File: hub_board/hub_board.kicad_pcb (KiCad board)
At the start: 4 copper layers, 75 x 75 mm, 16 parts, among them J1 Fingers, J2 Fingers, J3 Fingers, J4 Fingers, J5 1473149-4, J6 Test Points, J7 54-00166, U1 AP2112K-3.3TRG1

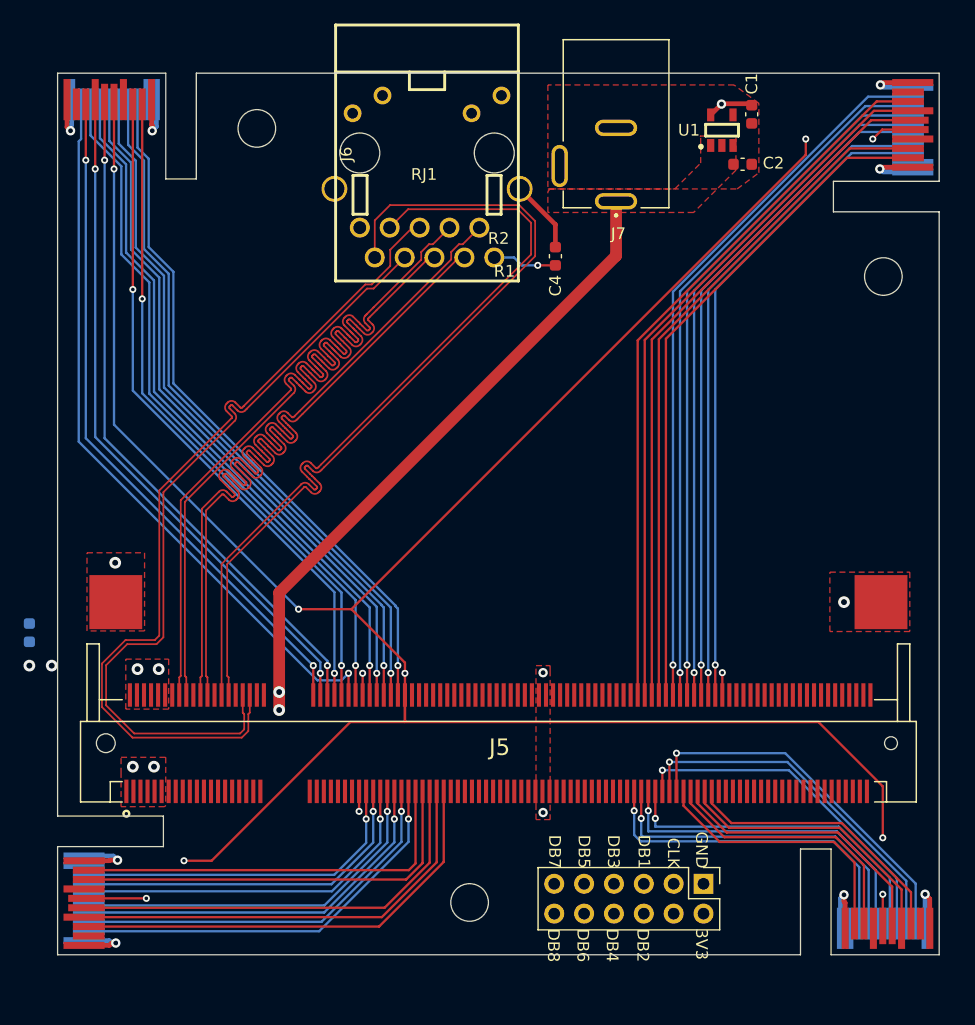
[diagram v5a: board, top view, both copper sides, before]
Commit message: Finish routing hub board
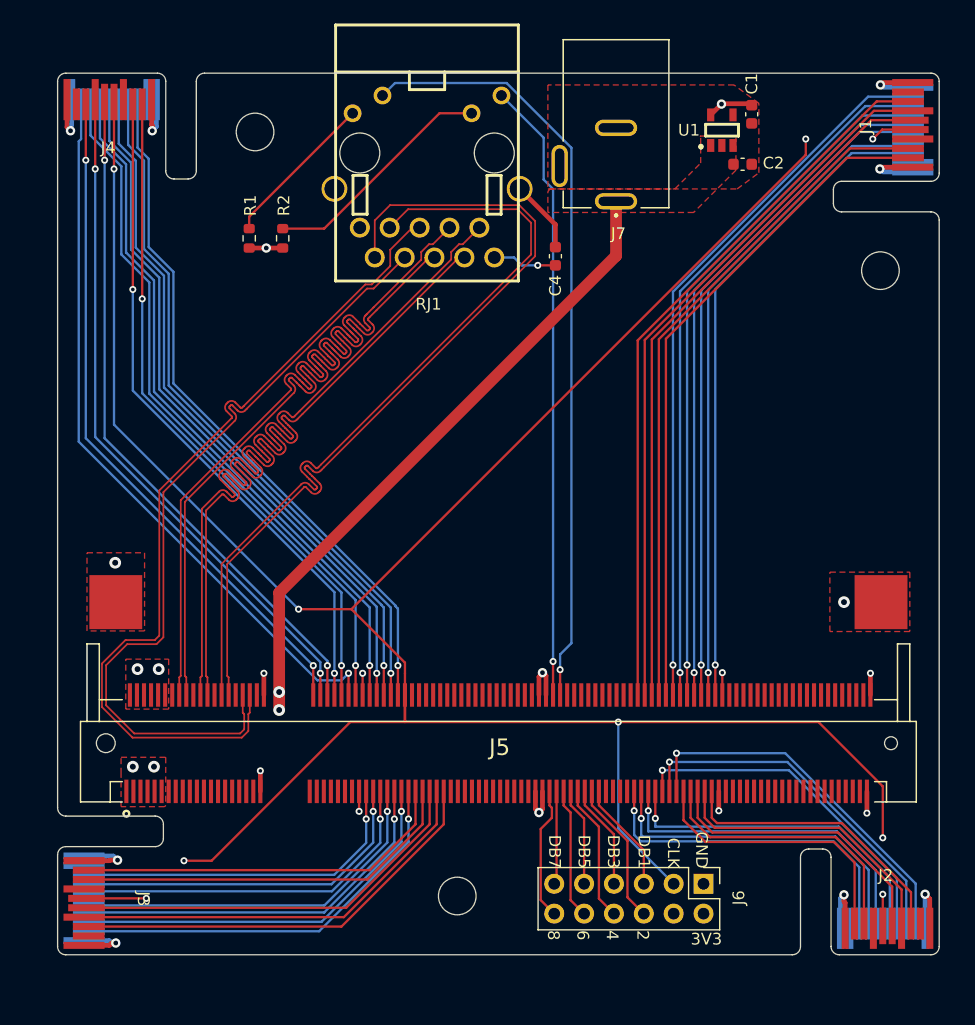
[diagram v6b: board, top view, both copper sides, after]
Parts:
- removed C3: 10u, Capacitor_SMD:C_0603_1608Metric
- added R1: 220, Resistor_SMD:R_0603_1608Metric, F.Cu at (16.3, 14.1)
- added R2: 220, Resistor_SMD:R_0603_1608Metric, F.Cu at (19.1, 14.1)
- moved REF** 1.19 mm to (34.0, 70.0)
- moved REF** 0.56 mm to (70.0, 16.8)
- moved REF** 0.34 mm to (16.8, 5.00)
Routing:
- net /LED1: track 0.00 -> 65.5 mm, vias 0 -> 1
- net /LED2: track 0.00 -> 53.1 mm, vias 0 -> 1
- net Net-(RJ1-LED2+): track 0.00 -> 20.1 mm
- net /CLK: track 220.1 -> 235.8 mm
- net GND: track 35.7 -> 51.0 mm, vias 13 -> 18
- net Net-(RJ1-LED1+): track 0.00 -> 13.5 mm
- net /DBG2: track 0.00 -> 12.2 mm
- net /DBG4: track 0.00 -> 11.7 mm
- net /DBG8: track 0.00 -> 11.4 mm
- net /DBG6: track 0.00 -> 11.1 mm
- net /DBG1: track 0.00 -> 9.44 mm
- net /DBG3: track 0.00 -> 8.89 mm
- net /DBG5: track 0.00 -> 8.33 mm
- net /DBG7: track 0.00 -> 7.94 mm
- net +3V3: track 26.6 -> 29.4 mm, vias 5 -> 6
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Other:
- outline, holes or cut-outs redrawn
- board text added: "2"
- board text added: "4"
- board text added: "6"
- board text added: "8"
- board text removed: "DB2"
- board text removed: "DB4"
- board text removed: "DB6"
- board text removed: "DB8"

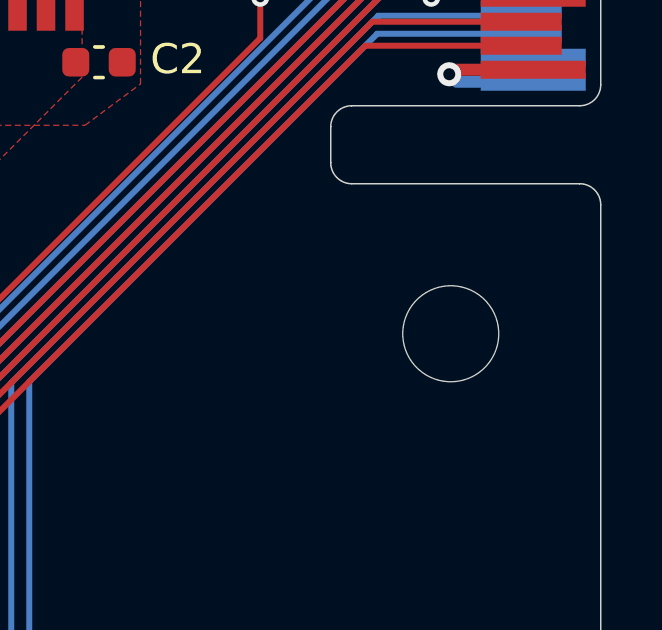
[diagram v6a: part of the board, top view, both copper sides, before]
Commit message: Fix solder mask gap size on DDR connector
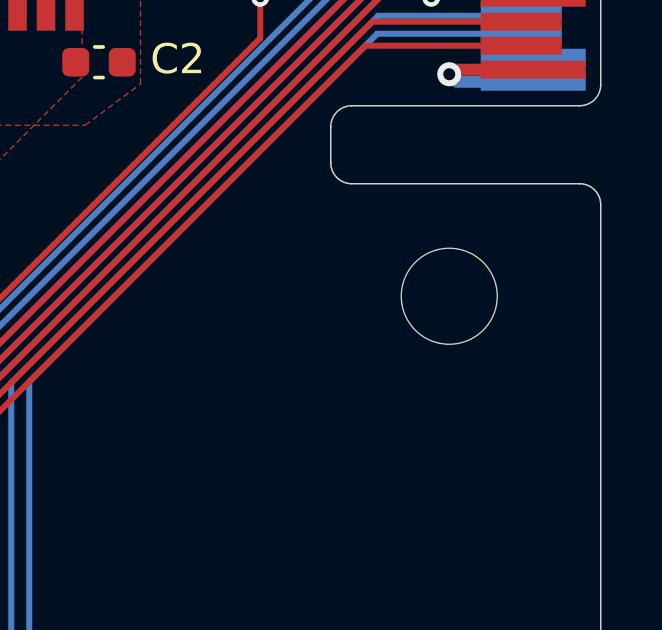
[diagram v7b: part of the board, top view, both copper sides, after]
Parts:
- moved REF** 1.25 mm to (70.0, 15.6)
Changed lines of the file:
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@@
 	(footprint "MountingHole:MountingHole_3.2mm_M3"
 		(layer "F.Cu")
-		(at 70 16.8)
+		(at 69.95 15.55)
 		(descr "Mounting Hole 3.2mm, M3, no annular, generated by kicad-footprint-generator mountinghole.py")
 		(tags "mountinghole M3")
@@
 			(at 25.859791 22.95 0)
 			(layer "F.Fab")
+			(hide yes)
 			(effects
 				(font
